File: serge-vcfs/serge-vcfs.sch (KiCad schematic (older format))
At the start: 88 parts, among them Q1 2N3904, Q2 2N3904, Q3 2N3904

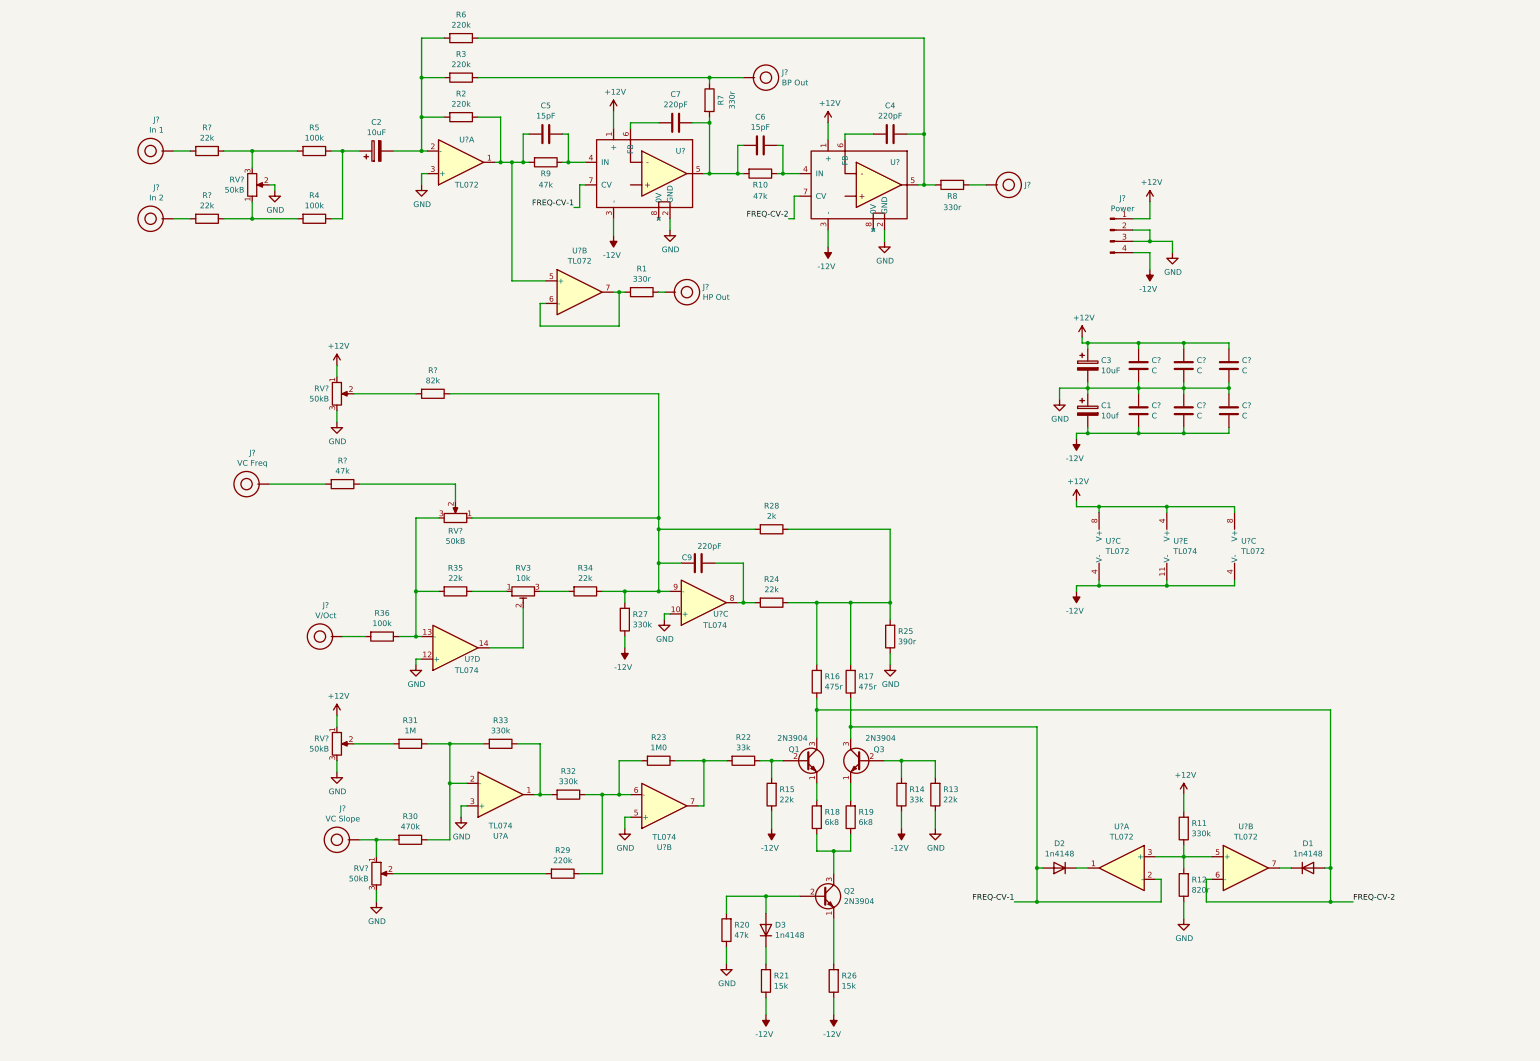
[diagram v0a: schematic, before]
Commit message: Fixing issue with vcfs
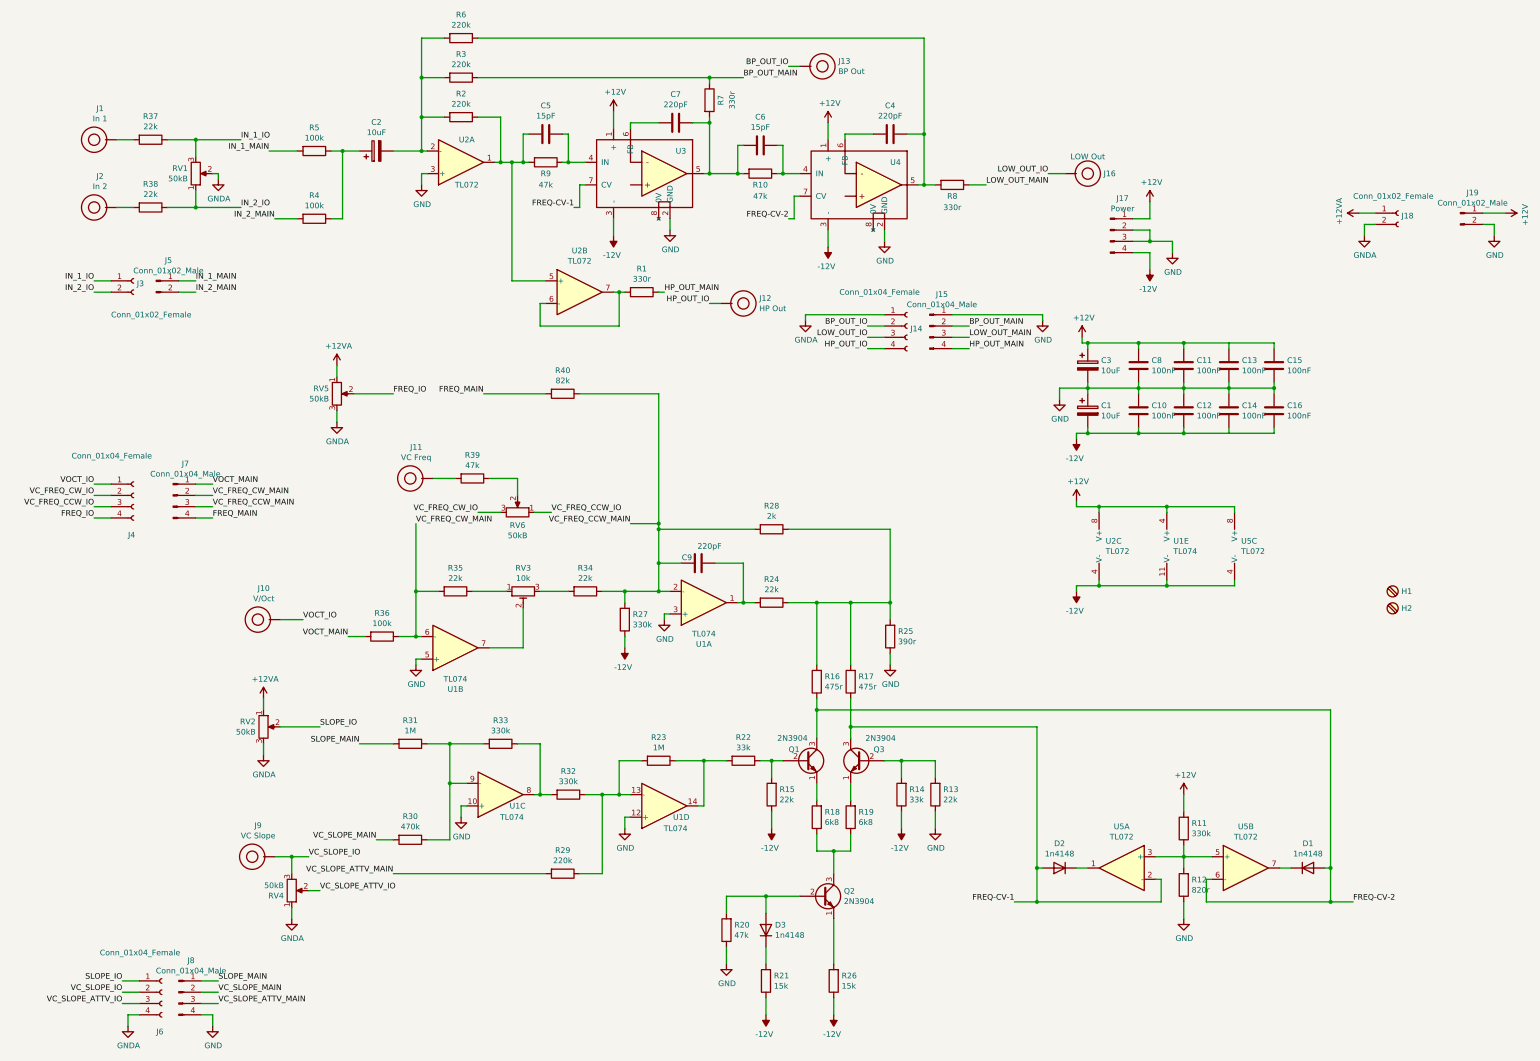
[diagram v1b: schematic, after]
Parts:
- added C15, C16: 100nF, rumblesan-footprints:C_Rect_L7.0mm_W3.5mm_P5.00mm, symbol Device:C
- added H1, H2: MountingScrew_M3_Flathead, MountingHole:MountingHole_3.2mm_M3, symbol Board_Hardware:MountingScrew_M3_Flathead
- added J14, J4, J6: Conn_01x04_Female, Connector_PinHeader_2.54mm:PinHeader_1x04_P2.54mm_Vertical, symbol Connector:Conn_01x04_Female
- added J15, J7, J8: Conn_01x04_Male, Connector_PinSocket_2.54mm:PinSocket_1x04_P2.54mm_Vertical, symbol Connector:Conn_01x04_Male
- added J18: Conn_01x02_Female, Connector_PinSocket_2.54mm:PinSocket_1x02_P2.54mm_Vertical, symbol Connector:Conn_01x02_Female
- added J19: Conn_01x02_Male, Connector_PinHeader_2.54mm:PinHeader_1x02_P2.54mm_Vertical, symbol Connector:Conn_01x02_Male
- added J3: Conn_01x02_Female, Connector_PinHeader_2.54mm:PinHeader_1x02_P2.54mm_Vertical, symbol Connector:Conn_01x02_Female
- added J5: Conn_01x02_Male, Connector_PinSocket_2.54mm:PinSocket_1x02_P2.54mm_Vertical, symbol Connector:Conn_01x02_Male
- C1: value 10uf -> 10uF; footprint (none) -> rumblesan-footprints:CP_Radial_D5.0mm_P2.50mm
- C10, C11, C12, C13, C14, C8: renamed from C?; value C -> 100nF; footprint (none) -> rumblesan-footprints:C_Rect_L7.0mm_W3.5mm_P5.00mm
- C2, C3: footprint (none) -> rumblesan-footprints:CP_Radial_D5.0mm_P2.50mm
- C4, C7: footprint (none) -> rumblesan-footprints:C_Axial_L12.0mm_D5.0mm_P15.00mm_Horizontal
- C5, C6, C9: footprint (none) -> rumblesan-footprints:C_Rect_L7.0mm_W3.5mm_P5.00mm
- D1, D2, D3: footprint (none) -> rumblesan-footprints:Diode_THT_P7.62mm_Horizontal
- J1, J10, J11, J12, J13, J2, J9: renamed from J?; footprint (none) -> rumblesan-footprints:BananaJack_THT_JohnsonCinch_108-09
- J16: renamed from J?; value BananaJack_PanelMount -> LOW Out; footprint (none) -> rumblesan-footprints:BananaJack_THT_JohnsonCinch_108-09
- J17: renamed from J?; footprint (none) -> rumblesan-footprints:Molex_KK-254_AE-6410-04A_1x04_P2.54mm_Vertical
- R1, R10, R11, R12, R13, R14, R15, R16, R17, R18, R19, R2, R20, R21, R22, R24, R25, R26, R27, R28, R29, R3, R30, R31, R32, R33, R34, R35, R36, R4, R5, R6, R7, R8, R9: footprint (none) -> rumblesan-footprints:R_Axial_DIN0207_L6.3mm_D2.5mm_P7.62mm_Horizontal
- R23: value 1M0 -> 1M; footprint (none) -> rumblesan-footprints:R_Axial_DIN0207_L6.3mm_D2.5mm_P7.62mm_Horizontal
- R37, R38, R39, R40: renamed from R?; footprint (none) -> rumblesan-footprints:R_Axial_DIN0207_L6.3mm_D2.5mm_P7.62mm_Horizontal
- RV1, RV2, RV4, RV5, RV6: renamed from RV?; footprint (none) -> rumblesan-footprints:Potentiometer_Alpha_RD901F-40-00D_Single_Vertical_CircularHoles
- RV3: footprint (none) -> rumblesan-footprints:Potentiometer_THT_Bourns_3306P_Vertical
- U1: renamed from U?; footprint (none) -> rumblesan-footprints:DIP-14_W7.62mm_Socket
- U2, U5: renamed from U?; footprint (none) -> rumblesan-footprints:DIP-8_W7.62mm_Socket
- U3, U4: renamed from U?; footprint (none) -> rumblesan-footprints:Serge_GainCell_Vertical
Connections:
- net +12V: now also C15.1, J19.1 (Pin_1); no longer RV2.1, RV5.1
- net -12V: now also C16.2
- net GND: now also C15.2, C16.1, J15.1 (Pin_1), J19.2 (Pin_2), J8.4 (Pin_4); no longer RV1.2, RV2.3, RV4.3, RV5.3
- net VOCT_IO: now reaches J10.1
- net VOCT_IO: now also J4.1 (Pin_1); no longer R36.2
- net IN_1_IO: now reaches R37.1, RV1.3
- net IN_1_IO: now also J3.1 (Pin_1); no longer R5.2
- net IN_2_IO: now reaches R38.1, RV1.1
- net IN_2_IO: now also J3.2 (Pin_2); no longer R4.2
- net HP_OUT_IO: now reaches J12.1
- net HP_OUT_IO: now also J14.4 (Pin_4); no longer R1.1
- net BP_OUT_MAIN: now reaches R3.1, R7.1
- net BP_OUT_MAIN: now also J15.2 (Pin_2); no longer J13.1
- net LOW_OUT_IO: now reaches J16.1
- net LOW_OUT_IO: now also J14.3 (Pin_3); no longer R8.1
- net at R32.2, R33.1: now also U1.8; no longer U1.1
- net at R30.1, R31.1, R33.2: now also U1.9 (-); no longer U1.2 (-)
- net at R23.2, R29.1, R32.1: now also U1.13 (-); no longer U1.6 (-)
- net at R22.2, R23.1: now also U1.14; no longer U1.7
- net at C9.1, R24.2: now also U1.1; no longer U1.8
- net VC_FREQ_CCW_MAIN: now reaches C9.2, R27.2, R28.2, R34.1, R40.1
- net VC_FREQ_CCW_MAIN: now also U1.2 (-), J7.3 (Pin_3); no longer RV6.1, U1.9 (-)
- net VC_FREQ_CW_MAIN: now reaches R35.2, R36.1
- net VC_FREQ_CW_MAIN: now also U1.6 (-), J7.2 (Pin_2); no longer RV6.3, U1.13 (-)
- net at RV3.2: now also U1.7; no longer U1.14
- net VC_SLOPE_ATTV_IO: now reaches RV4.2
- net VC_SLOPE_ATTV_IO: now also J6.3 (Pin_3); no longer R29.2
- net SLOPE_IO: now reaches RV2.2
- net SLOPE_IO: now also J6.1 (Pin_1); no longer R31.2
- net FREQ_IO: now reaches RV5.2
- net FREQ_IO: now also J4.4 (Pin_4); no longer R40.2
- new net +12VA: J18.1 (Pin_1), RV2.1, RV5.1
- new net BP_OUT_IO: J13.1, J14.2 (Pin_2)
- new net FREQ_MAIN: J7.4 (Pin_4), R40.2
- new net GNDA: J14.1 (Pin_1), J18.2 (Pin_2), J6.4 (Pin_4), RV1.2, RV2.3, RV4.1, RV5.3
- new net HP_OUT_MAIN: J15.4 (Pin_4), R1.1
- new net IN_1_MAIN: J5.1 (Pin_1), R5.2
- new net IN_2_MAIN: J5.2 (Pin_2), R4.2
- new net LOW_OUT_MAIN: J15.3 (Pin_3), R8.1
- new net SLOPE_MAIN: J8.1 (Pin_1), R31.2
- new net VC_FREQ_CCW_IO: J4.3 (Pin_3), RV6.1
- new net VC_FREQ_CW_IO: J4.2 (Pin_2), RV6.3
- new net VC_SLOPE_ATTV_MAIN: J8.3 (Pin_3), R29.2
- new net VC_SLOPE_IO: J6.2 (Pin_2), J9.1, RV4.3
- new net VC_SLOPE_MAIN: J8.2 (Pin_2), R30.2
- new net VOCT_MAIN: J7.1 (Pin_1), R36.2
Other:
- moved on the sheet: J1, J10, J11, J12, J13, J16, J2, J9, R37, R38, R39, R40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
